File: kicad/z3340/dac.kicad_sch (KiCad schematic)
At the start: 29 parts, among them U12 AD5328, U5 TL074, U6 LM4040AIM3-2.5

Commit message: cleaning up and rename dir to z3340
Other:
- moved on the sheet: C25, C28, C33, C34, C36, R17, U6

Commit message: cleanup references after file renaming
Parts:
- U12: symbol as3340:AD5328 -> z3340:AD5328
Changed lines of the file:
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@@
     )
   )
-  (symbol (lib_id "as3340:AD5328") (at 100.33 71.12 0) (unit 1)
+  (symbol (lib_id "z3340:AD5328") (at 100.33 71.12 0) (unit 1)
     (in_bom yes) (on_board yes) (dnp no)
     (property "Reference" "U12" (at 99.06 71.12 0)

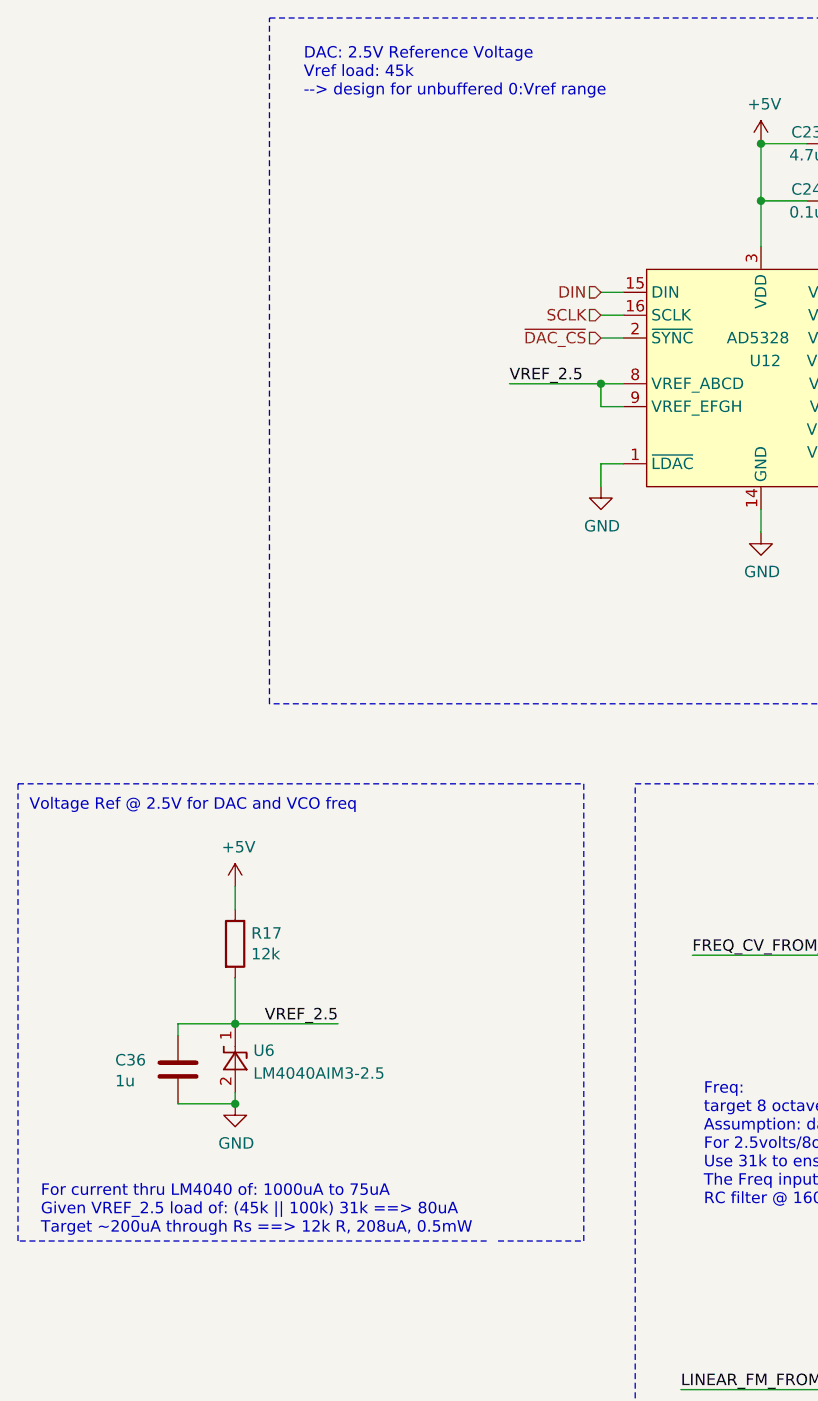
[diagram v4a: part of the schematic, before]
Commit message: checkpoint for z3340 v0.9.  Fixed lm4040 resistor, exp modulation level; removed polygons from routing
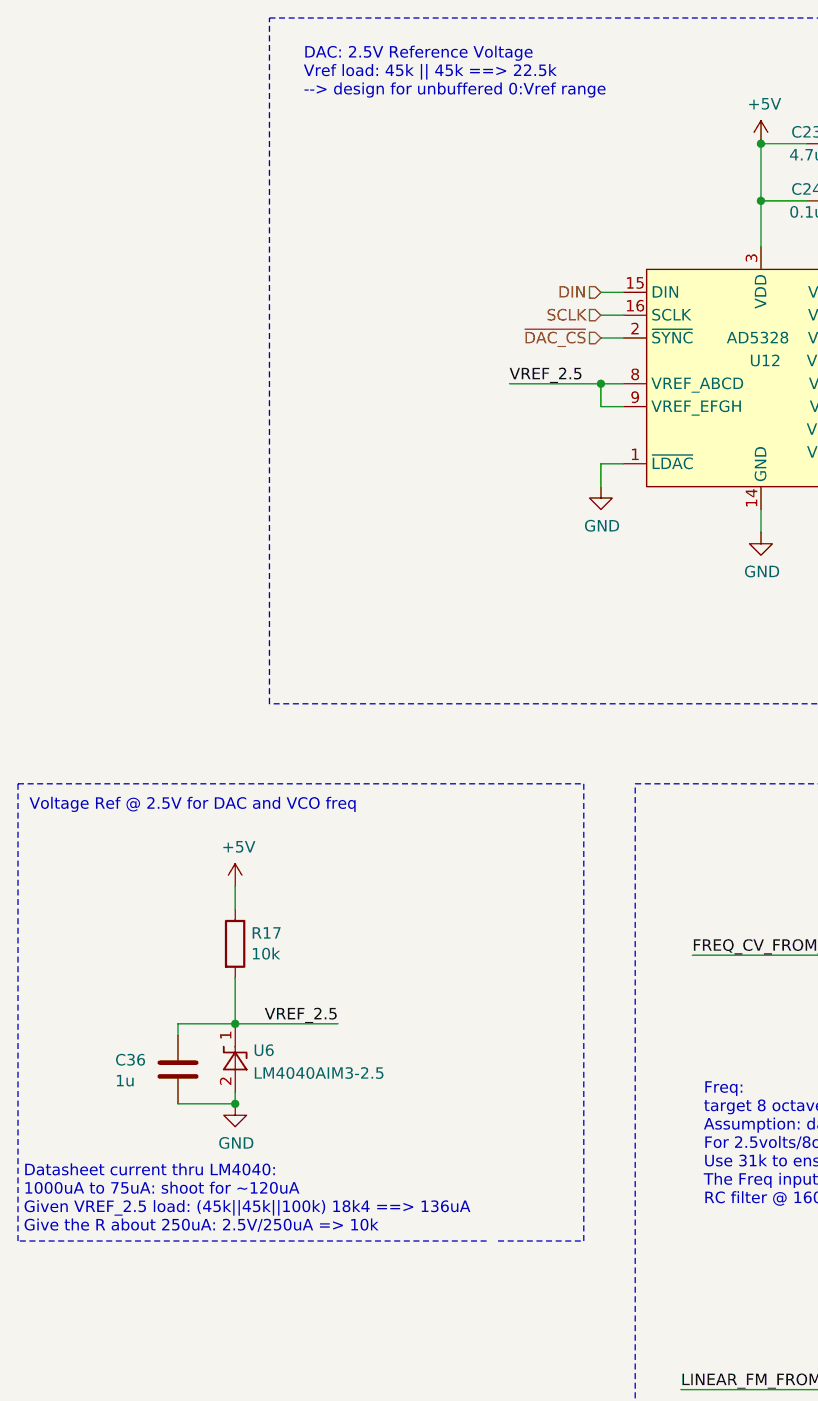
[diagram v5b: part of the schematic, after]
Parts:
- R17: value 12k -> 10k; LCSC Part C22790 -> C25804
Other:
- note added: "DAC: 2.5V Reference Voltage Vref load: 45k || 45k ==> 22.5k --> design for unbuffered 0:Vref range"
- note added: "Datasheet current thru LM4040: 1000uA to 75uA: shoot for ~120uA Given VREF_2.5 load: (45k||45k||100k) 18k4 ==> 136uA Give the R about 250uA: 2.5V/250uA => 10k"
- note removed: "DAC: 2.5V Reference Voltage Vref load: 45k --> design for unbuffered 0:Vref range"
- note removed: "For current thru LM4040 of: 1000uA to 75uA Given VREF_2.5 load of: (45k || 100k) 31k ==> 80uA Target ~200uA through Rs ==> 12k R, 208uA, 0.5mW"
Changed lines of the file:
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@@
     (effects (font (size 1.27 1.27)) (justify left bottom))
   )
-  (text "For current thru LM4040 of: 1000uA to 75uA\nGiven VREF_2.5 load of: (45k || 100k) 31k ==> 80uA\nTarget ~200uA through Rs ==> 12k R, 208uA, 0.5mW\n"
-    (at 20.32 168.275 0)
+  (text "Datasheet current thru LM4040:\n1000uA to 75uA: shoot for ~120uA\nGiven VREF_2.5 load: (45k||45k||100k) 18k4 ==> 136uA\nGive the R about 250uA: 2.5V/250uA => 10k\n\n"
+    (at 18.415 170.18 0)
     (effects (font (size 1.27 1.27)) (justify left bottom))
   )
@@
     (effects (font (size 1.27 1.27)) (justify left bottom))
   )
-  (text "DAC: 2.5V Reference Voltage\nVref load: 45k\n--> design for unbuffered 0:Vref range"
+  (text "DAC: 2.5V Reference Voltage\nVref load: 45k || 45k ==> 22.5k\n--> design for unbuffered 0:Vref range"
     (at 49.53 41.91 0)
     (effects (font (size 1.27 1.27)) (justify left bottom))
@@
       (effects (font (size 1.27 1.27)) (justify left))
     )
-    (property "Value" "12k" (at 43.688 137.033 0)
+    (property "Value" "10k" (at 43.688 137.033 0)
       (effects (font (size 1.27 1.27)) (justify left))
     )
@@
       (effects (font (size 1.27 1.27)) hide)
     )
-    (property "LCSC Part" "C22790" (at 41.91 135.89 0)
-      (effects (font (size 1.27 1.27)) hide)
-    )
+    (property "LCSC Part" "C25804" (at 41.91 135.89 0)
+      (effects (font (size 1.27 1.27)) hide)
+    )

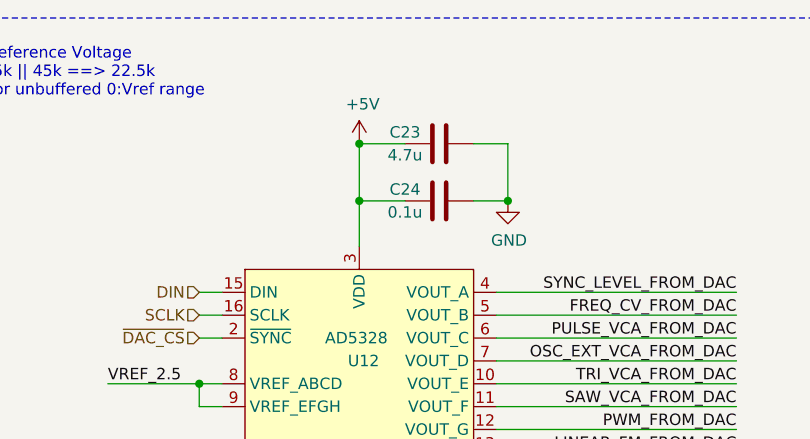
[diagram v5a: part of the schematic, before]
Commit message: updates for v0.9: polygons, LED resistor, mod amount
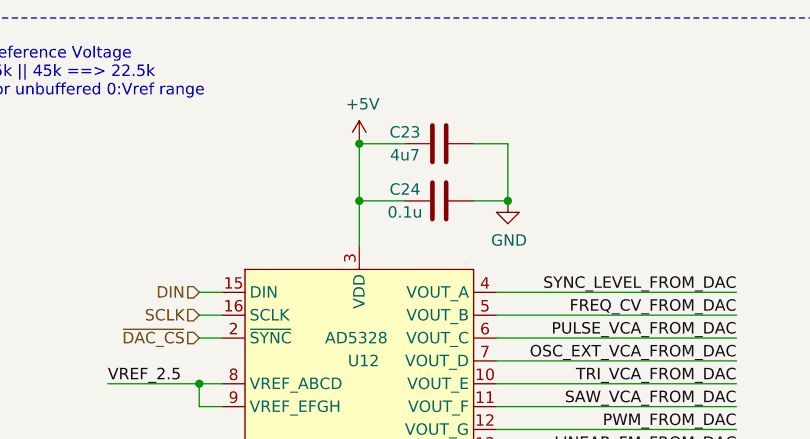
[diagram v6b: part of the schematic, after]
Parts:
- C15: LCSC (none) -> C53987; LCSC Part C53987 -> (none)
- C16: LCSC (none) -> C1588; LCSC Part C1588 -> (none)
- C23: value 4.7u -> 4u7; LCSC (none) -> C1779; LCSC Part C1779 -> (none)
- C24, C32: LCSC (none) -> C14663; LCSC Part C14663 -> (none)
- C25, C28, C33, C34, C35: LCSC (none) -> C21122; LCSC Part C21122 -> (none)
- C36: LCSC (none) -> C15849; LCSC Part C15849 -> (none)
- R10: LCSC (none) -> C23196; LCSC Part C23196 -> (none)
- R14, R16: LCSC (none) -> C25803; LCSC Part C25803 -> (none)
- R17: LCSC (none) -> C25804; LCSC Part C25804 -> (none)
- R18, R36, R39, R43, R47: LCSC (none) -> C4216; LCSC Part C4216 -> (none)
- R30, R33, R44, R46: LCSC (none) -> C25981; LCSC Part C25981 -> (none)
- R41: LCSC (none) -> C21190; LCSC Part C21190 -> (none)
- R42: LCSC (none) -> C23189; LCSC Part C23189 -> (none)
- U12: LCSC (none) -> C29162; LCSC Part C29162 -> (none)
- U5: LCSC (none) -> C96507; LCSC Part C96507 -> (none)
- U6: LCSC (none) -> C460725; LCSC Part C460725 -> (none)
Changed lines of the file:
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@@
   (title_block
     (title "Zoxnoxious 3340 Oscillator")
-    (date "2024-07-15")
-    (rev "0.8")
+    (date "2025-02-06")
+    (rev "0.9")
     (company "Zoxnoxious Engineering")
   )
@@
       (effects (font (size 1.27 1.27)) hide)
     )
-    (property "LCSC Part" "C21190" (at 118.11 137.16 0)
+    (property "LCSC" "C21190" (at 118.11 137.16 0)
       (effects (font (size 1.27 1.27)) hide)
     )
@@
       (effects (font (size 1.27 1.27)))
     )
-    (property "Value" "4.7u" (at 105.41 48.26 90)
+    (property "Value" "4u7" (at 105.41 48.26 90)
       (effects (font (size 1.27 1.27)))
     )
@@
       (effects (font (size 1.27 1.27)) hide)
     )
-    (property "LCSC Part" "C1779" (at 109.22 46.99 0)
+    (property "LCSC" "C1779" (at 109.22 46.99 0)
       (effects (font (size 1.27 1.27)) hide)
     )
@@
       (effects (font (size 1.27 1.27)) hide)
     )
-    (property "LCSC Part" "C14663" (at 109.22 53.34 0)
+    (property "LCSC" "C14663" (at 109.22 53.34 0)
       (effects (font (size 1.27 1.27)) hide)
     )
@@
       (effects (font (size 1.27 1.27)) hide)
     )
-    (property "LCSC Part" "C4216" (at 245.11 58.42 0)
+    (property "LCSC" "C4216" (at 245.11 58.42 0)
       (effects (font (size 1.27 1.27)) hide)
     )
@@
       (effects (font (size 1.27 1.27)) hide)
     )
-    (property "LCSC Part" "C23196" (at 261.62 52.07 0)
+    (property "LCSC" "C23196" (at 261.62 52.07 0)
       (effects (font (size 1.27 1.27)) hide)
     )
@@
       (effects (font (size 1.27 1.27)) hide)
     )
-    (property "LCSC Part" "C25981" (at 248.92 110.49 0)
+    (property "LCSC" "C25981" (at 248.92 110.49 0)
       (effects (font (size 1.27 1.27)) hide)
     )
@@
       (effects (font (size 1.27 1.27)) hide)
     )
-    (property "LCSC Part" "C4216" (at 257.81 116.84 0)
+    (property "LCSC" "C4216" (at 257.81 116.84 0)
       (effects (font (size 1.27 1.27)) hide)
     )
@@
       (effects (font (size 1.27 1.27)) hide)
     )
-    (property "LCSC Part" "C25981" (at 248.92 135.89 0)
+    (property "LCSC" "C25981" (at 248.92 135.89 0)
       (effects (font (size 1.27 1.27)) hide)
     )
@@
       (effects (font (size 1.27 1.27)) hide)
     )
-    (property "LCSC Part" "C4216" (at 257.81 142.24 0)
+    (property "LCSC" "C4216" (at 257.81 142.24 0)
       (effects (font (size 1.27 1.27)) hide)
     )
@@
       (effects (font (size 1.27 1.27)) hide)
     )
-    (property "LCSC Part" "C21122" (at 267.97 166.37 0)
+    (property "LCSC" "C21122" (at 267.97 166.37 0)
       (effects (font (size 1.27 1.27)) hide)
     )
@@
       (effects (font (size 1.27 1.27)) hide)
     )
-    (property "LCSC Part" "C15849" (at 35.56 149.86 0)
+    (property "LCSC" "C15849" (at 35.56 149.86 0)
       (effects (font (size 1.27 1.27)) hide)
     )
@@
       (effects (font (size 1.27 1.27)) hide)
     )
-    (property "LCSC Part" "C25803" (at 332.74 58.42 0)
+    (property "LCSC" "C25803" (at 332.74 58.42 0)
       (effects (font (size 1.27 1.27)) hide)
     )
@@
       (effects (font (size 1.27 1.27)) hide)
     )
-    (property "LCSC Part" "C25804" (at 41.91 135.89 0)
+    (property "LCSC" "C25804" (at 41.91 135.89 0)
       (effects (font (size 1.27 1.27)) hide)
     )
@@
       (effects (font (size 1.27 1.27)) hide)
     )
-    (property "LCSC Part" "C21122" (at 266.7 116.84 0)
+    (property "LCSC" "C21122" (at 266.7 116.84 0)
       (effects (font (size 1.27 1.27)) hide)
     )
@@
       (effects (font (size 1.27 1.27)) hide)
     )
-    (property "LCSC Part" "C23189" (at 119.38 185.42 0)
+    (property "LCSC" "C23189" (at 119.38 185.42 0)
       (effects (font (size 1.27 1.27)) hide)
     )
@@
       (effects (font (size 1.27 1.27)) hide)
     )
-    (property "LCSC Part" "C21122" (at 266.7 142.24 0)
+    (property "LCSC" "C21122" (at 266.7 142.24 0)
       (effects (font (size 1.27 1.27)) hide)
     )
@@
       (effects (font (size 1.27 1.27)) hide)
     )
-    (property "LCSC Part" "C25803" (at 349.25 52.07 0)
+    (property "LCSC" "C25803" (at 349.25 52.07 0)
       (effects (font (size 1.27 1.27)) hide)
     )
@@
       (effects (font (size 1.27 1.27)) hide)
     )
-    (property "LCSC Part" "C25981" (at 250.19 184.15 0)
+    (property "LCSC" "C25981" (at 250.19 184.15 0)
       (effects (font (size 1.27 1.27)) hide)
     )
@@
       (effects (font (size 1.27 1.27)) hide)
     )
-    (property "LCSC Part" "C1588" (at 349.25 41.91 0)
+    (property "LCSC" "C1588" (at 349.25 41.91 0)
       (effects (font (size 1.27 1.27)) hide)
     )
@@
       (effects (font (size 1.27 1.27)) hide)
     )
-    (property "LCSC Part" "C29162" (at 100.33 71.12 0)
+    (property "LCSC" "C29162" (at 100.33 71.12 0)
       (effects (font (size 1.27 1.27)) hide)
     )
@@
       (effects (font (size 1.27 1.27)) hide)
     )
-    (property "LCSC Part" "C21122" (at 128.27 191.77 0)
+    (property "LCSC" "C21122" (at 128.27 191.77 0)
       (effects (font (size 1.27 1.27)) hide)
     )
@@
       (effects (font (size 1.27 1.27)) hide)
     )
-    (property "LCSC Part" "C96507" (at 349.25 60.96 0)
+    (property "LCSC" "C96507" (at 349.25 60.96 0)
       (effects (font (size 1.27 1.27)) hide)
     )
@@
       (effects (font (size 1.27 1.27)) hide)
     )
-    (property "LCSC Part" "C4216" (at 259.08 190.5 0)
+    (property "LCSC" "C4216" (at 259.08 190.5 0)
       (effects (font (size 1.27 1.27)) hide)
     )
@@
       (effects (font (size 1.27 1.27) italic) hide)
     )
-    (property "LCSC Part" "C460725" (at 41.91 148.59 90)
+    (property "LCSC" "C460725" (at 41.91 148.59 90)
       (effects (font (size 1.27 1.27)) hide)
     )
@@
       (effects (font (size 1.27 1.27)) hide)
     )
-    (property "LCSC Part" "C96507" (at 261.62 60.96 0)
+    (property "LCSC" "C96507" (at 261.62 60.96 0)
       (effects (font (size 1.27 1.27)) hide)
     )
@@
       (effects (font (size 1.27 1.27)) hide)
     )
-    (property "LCSC Part" "C14663" (at 127 143.51 0)
+    (property "LCSC" "C14663" (at 127 143.51 0)
       (effects (font (size 1.27 1.27)) hide)
     )
@@
       (effects (font (size 1.27 1.27)) hide)
     )
-    (property "LCSC Part" "C25981" (at 250.19 160.02 0)
+    (property "LCSC" "C25981" (at 250.19 160.02 0)
       (effects (font (size 1.27 1.27)) hide)
     )
@@
       (effects (font (size 1.27 1.27)) hide)
     )
-    (property "LCSC Part" "C21122" (at 267.97 190.5 0)
+    (property "LCSC" "C21122" (at 267.97 190.5 0)
       (effects (font (size 1.27 1.27)) hide)
     )
@@
       (effects (font (size 1.27 1.27)) hide)
     )
-    (property "LCSC Part" "C53987" (at 261.62 41.91 0)
+    (property "LCSC" "C53987" (at 261.62 41.91 0)
       (effects (font (size 1.27 1.27)) hide)
     )
@@
       (effects (font (size 1.27 1.27)) hide)
     )
-    (property "LCSC Part" "C4216" (at 259.08 166.37 0)
-      (effects (font (size 1.27 1.27)) hide)
-    )
+    (property "LCSC" "C4216" (at 259.08 166.37 0)
+      (effects (font (size 1.27 1.27)) hide)
+    )
